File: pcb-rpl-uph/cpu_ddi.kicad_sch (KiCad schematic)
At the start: 3 parts, among them U5 RPL_UPH_FCBGA1744

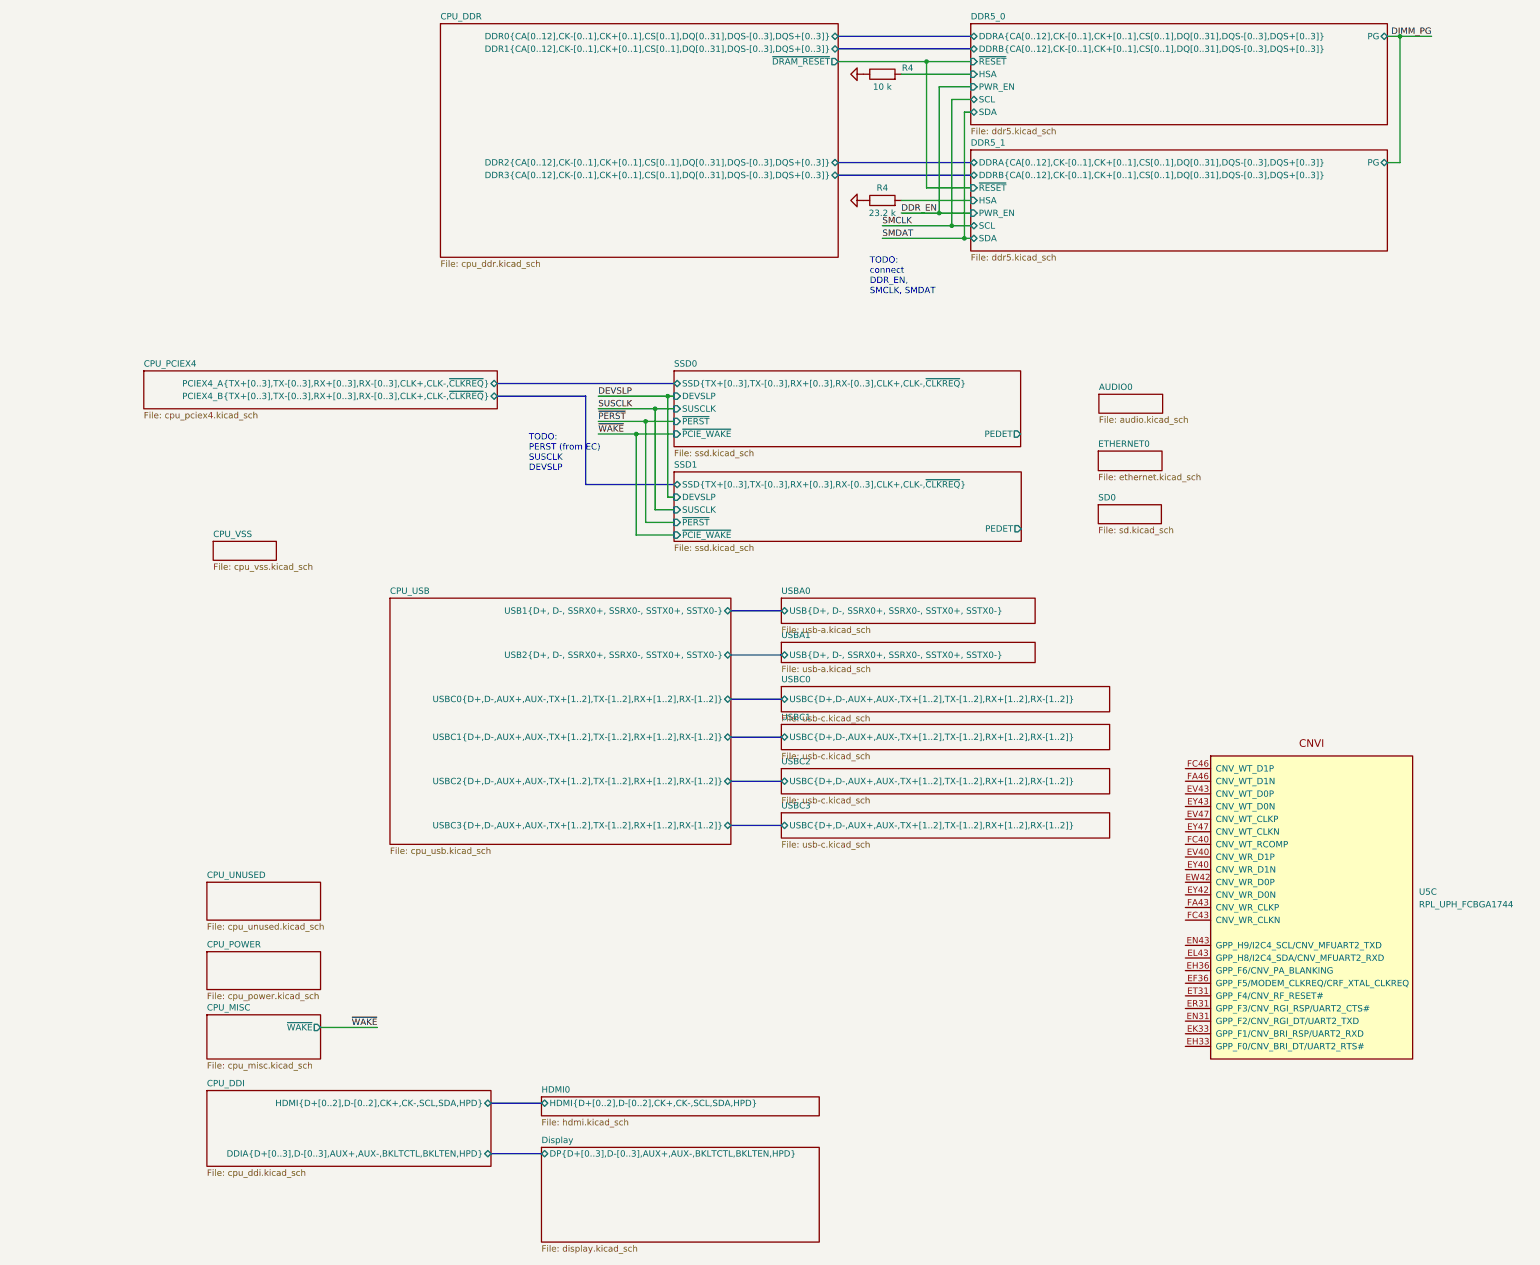
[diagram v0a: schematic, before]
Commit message: refactor much of CPU schematic symbol
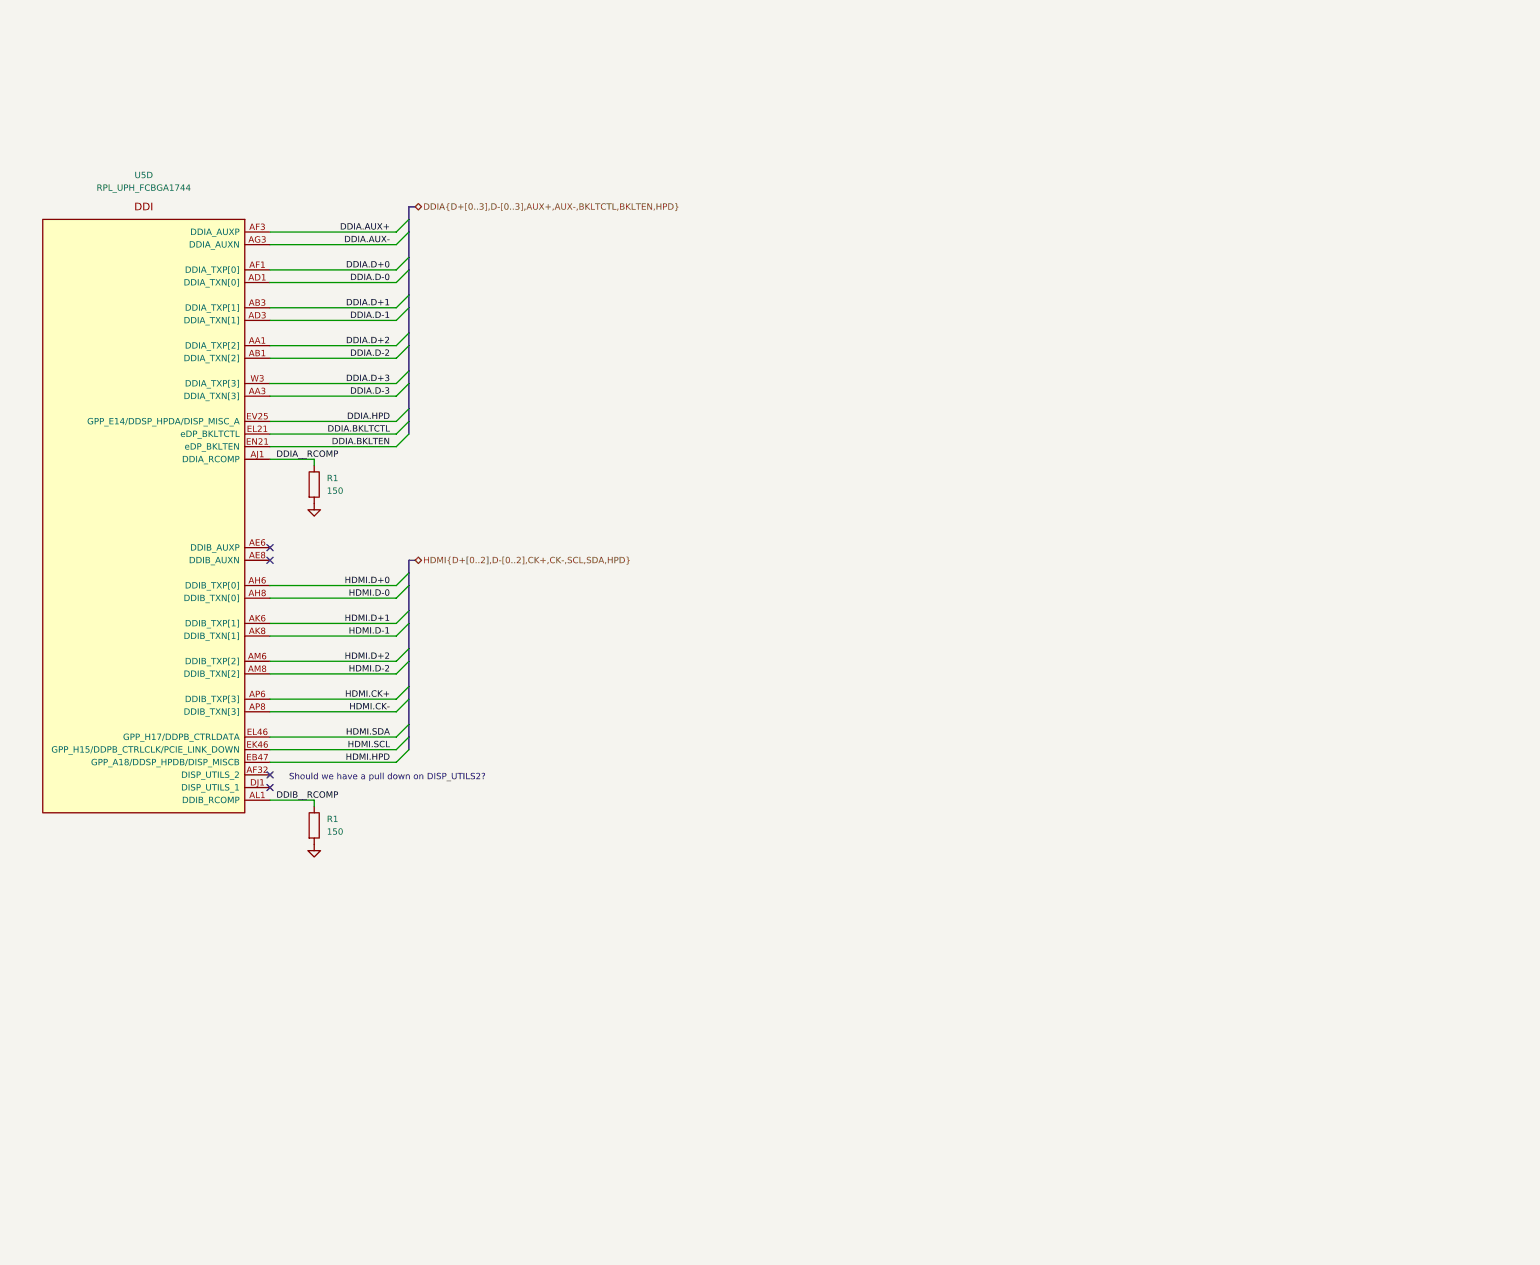
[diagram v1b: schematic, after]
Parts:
- removed R4: 23.2 k, local:R_0201_0603Metric, symbol Device:R
- removed R4: 10 k, local:R_0201_0603Metric, symbol Device:R
- removed U5: RPL_UPH_FCBGA1744, local:RPL_UPH_FCBGA1744, symbol local:RPL_UPH_FCBGA1744
- added R1 (x2): 150, local:R_0201_0603Metric, symbol Device:R
- added U5: RPL_UPH_FCBGA1744, local:RPL_UPH_FCBGA1744, symbol local:RPL_UPH_FCBGA1744
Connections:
- net GND: now also R1.2, R1.2
- new net DDIA.AUX+: U5.AF3 (DDIA_AUXP)
- new net DDIA.AUX-: U5.AG3 (DDIA_AUXN)
- new net DDIA.BKLTCTL: U5.EL21 (eDP_BKLTCTL)
- new net DDIA.BKLTEN: U5.EN21 (eDP_BKLTEN)
- new net DDIA.D+0: U5.AF1 (DDIA_TXP[0])
- new net DDIA.D+1: U5.AB3 (DDIA_TXP[1])
- new net DDIA.D+2: U5.AA1 (DDIA_TXP[2])
- new net DDIA.D+3: U5.W3 (DDIA_TXP[3])
- new net DDIA.D-0: U5.AD1 (DDIA_TXN[0])
- new net DDIA.D-1: U5.AD3 (DDIA_TXN[1])
- new net DDIA.D-2: U5.AB1 (DDIA_TXN[2])
- new net DDIA.D-3: U5.AA3 (DDIA_TXN[3])
- new net DDIA.HPD: U5.EV25 (GPP_E14/DDSP_HPDA/DISP_MISC_A)
- new net DDIA__RCOMP: R1.1, U5.AJ1 (DDIA_RCOMP)
- new net DDIB__RCOMP: R1.1, U5.AL1 (DDIB_RCOMP)
- new net HDMI.CK+: U5.AP6 (DDIB_TXP[3])
- new net HDMI.CK-: U5.AP8 (DDIB_TXN[3])
- new net HDMI.D+0: U5.AH6 (DDIB_TXP[0])
- new net HDMI.D+1: U5.AK6 (DDIB_TXP[1])
- new net HDMI.D+2: U5.AM6 (DDIB_TXP[2])
- new net HDMI.D-0: U5.AH8 (DDIB_TXN[0])
- new net HDMI.D-1: U5.AK8 (DDIB_TXN[1])
- new net HDMI.D-2: U5.AM8 (DDIB_TXN[2])
- new net HDMI.HPD: U5.EB47 (GPP_A18/DDSP_HPDB/DISP_MISCB)
- new net HDMI.SCL: U5.EK46 (GPP_H15/DDPB_CTRLCLK/PCIE_LINK_DOWN)
- new net HDMI.SDA: U5.EL46 (GPP_H17/DDPB_CTRLDATA)
- no-connect marks 0 -> 4
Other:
- removed sheet AUDIO0
- removed sheet CPU_DDI
- removed sheet CPU_DDR
- removed sheet CPU_MISC
- removed sheet CPU_PCIEX4
- removed sheet CPU_POWER
- removed sheet CPU_UNUSED
- removed sheet CPU_USB
- removed sheet CPU_VSS
- removed sheet DDR5_0
- removed sheet DDR5_1
- removed sheet Display
- removed sheet ETHERNET0
- removed sheet HDMI0
- removed sheet SD0
- removed sheet SSD0
- removed sheet SSD1
- removed sheet USBA0
- removed sheet USBA1
- removed sheet USBC0
- removed sheet USBC1
- removed sheet USBC2
- removed sheet USBC3
- note added: "Should we have a pull down on DISP_UTILS2?"
- note removed: "TODO: PERST (from EC) SUSCLK DEVSLP"
- note removed: "TODO: connect DDR_EN, SMCLK, SMDAT"
